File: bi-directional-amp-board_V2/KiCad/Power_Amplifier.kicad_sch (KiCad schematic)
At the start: 23 parts

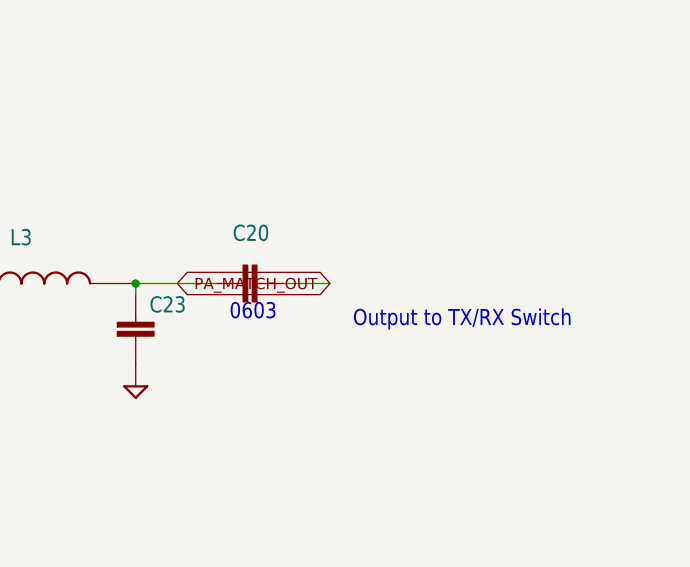
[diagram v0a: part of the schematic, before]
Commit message: re importing eagle files to kicad
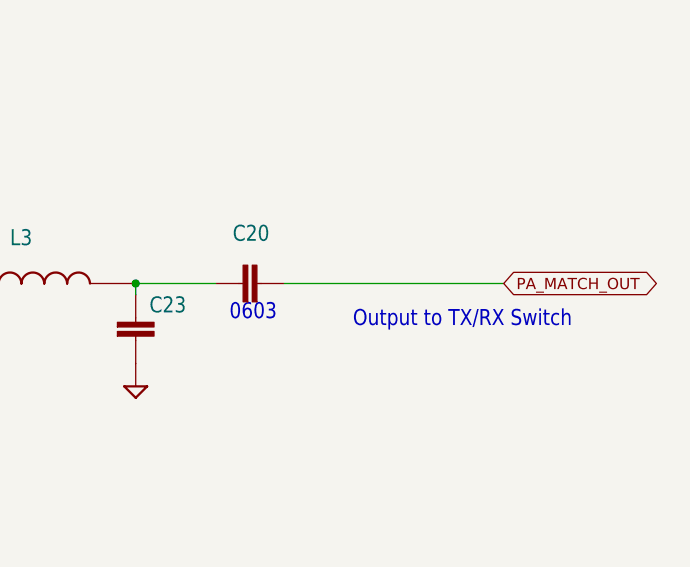
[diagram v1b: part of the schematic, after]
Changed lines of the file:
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@@
 (kicad_sch (version 20211123) (generator eeschema)
-  (paper "User" 490.22 254.406)
+  (paper "A2")
   (junction (at 105.918 114.3) (diameter 0) (color 0 0 0 0)
   )
@@
     (stroke (width 0) (type default) (color 0 0 0 0))
   )
-  (wire (pts (xy 219.456 114.3) (xy 224.536 114.3))
+  (wire (pts (xy 219.456 114.3) (xy 243.84 114.3))
     (stroke (width 0) (type default) (color 0 0 0 0))
   )
@@
     (effects (font (size 1.778 1.5113)) (justify left bottom))
   )
-  (global_label "PA_MATCH_OUT" (shape bidirectional) (at 224.536 114.3 180) (fields_autoplaced)
-    (effects (font (size 1.2446 1.2446)) (justify right))
-    (property "Intersheet References" "${INTERSHEET_REFS}" (id 0) (at 413.512 0 0)
+  (global_label "PA_MATCH_OUT" (shape bidirectional) (at 243.84 114.3 0) (fields_autoplaced)
+    (effects (font (size 1.2446 1.2446)) (justify left))
+    (property "Intersheet References" "${INTERSHEET_REFS}" (id 0) (at 54.864 228.6 0)
       (effects (font (size 1.27 1.27)) hide)
     )

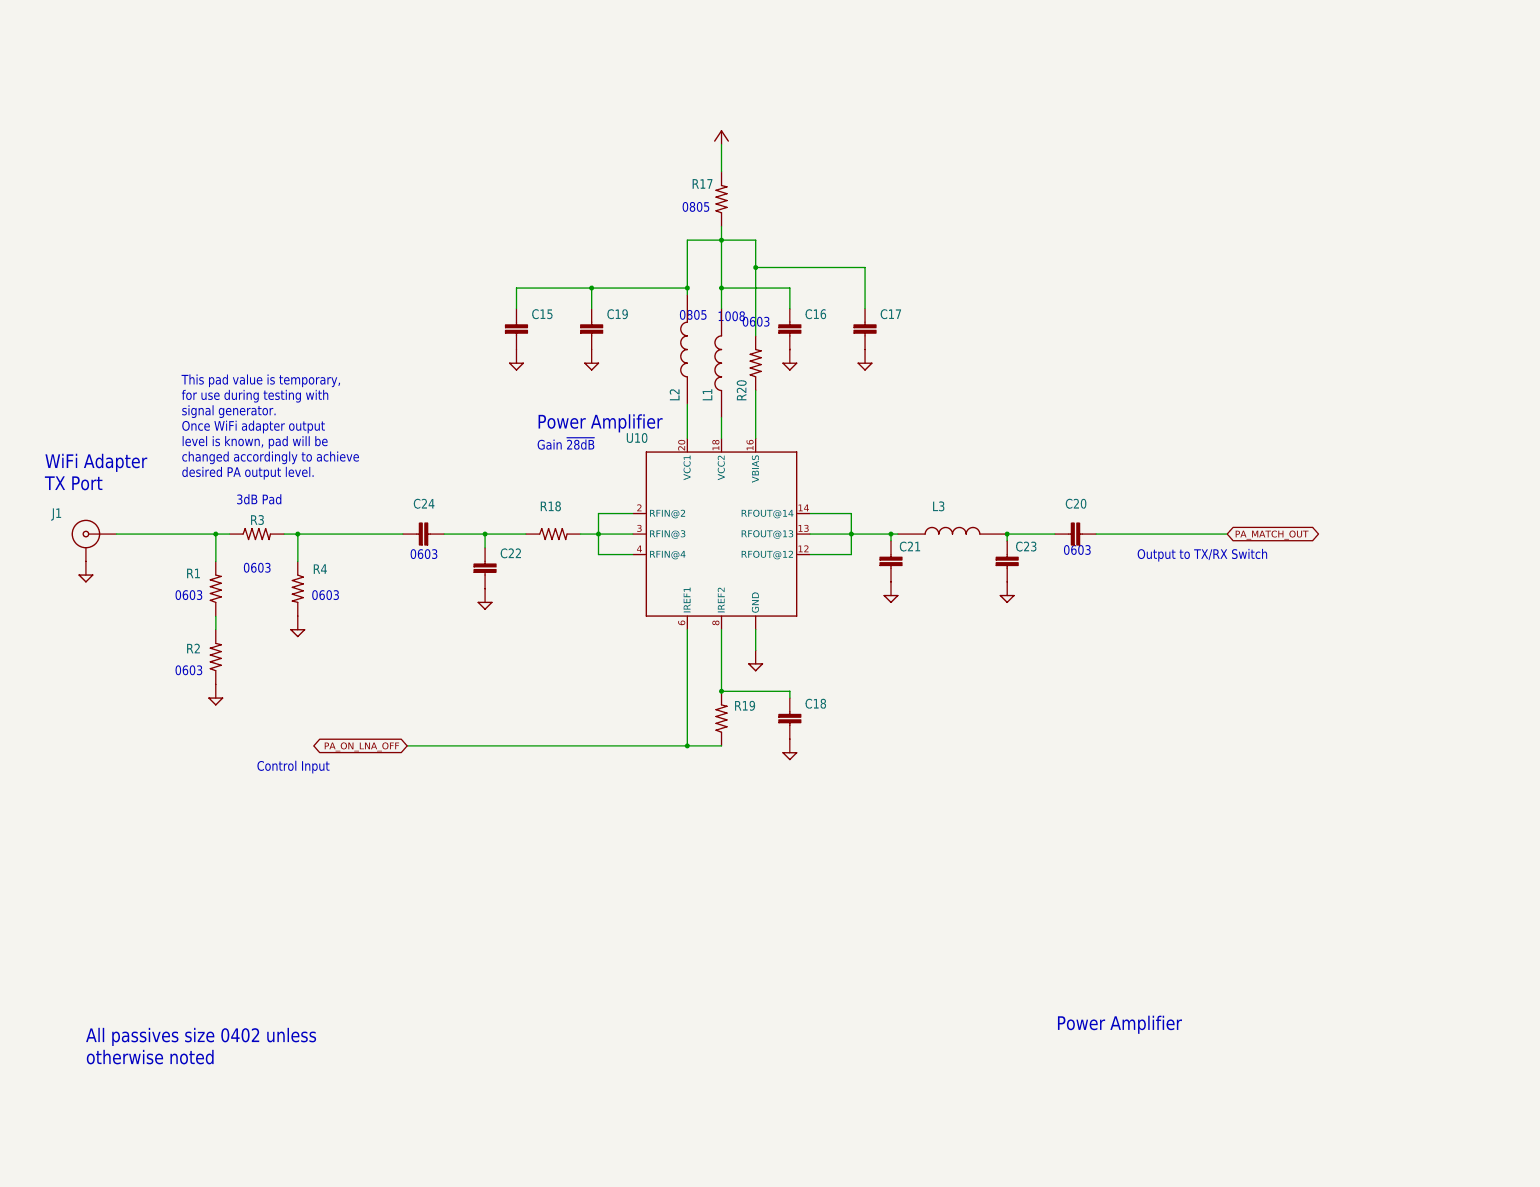
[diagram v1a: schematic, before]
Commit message: Updated KiCAD import of bidirectional amplifier. Still a bit broken, but better now.
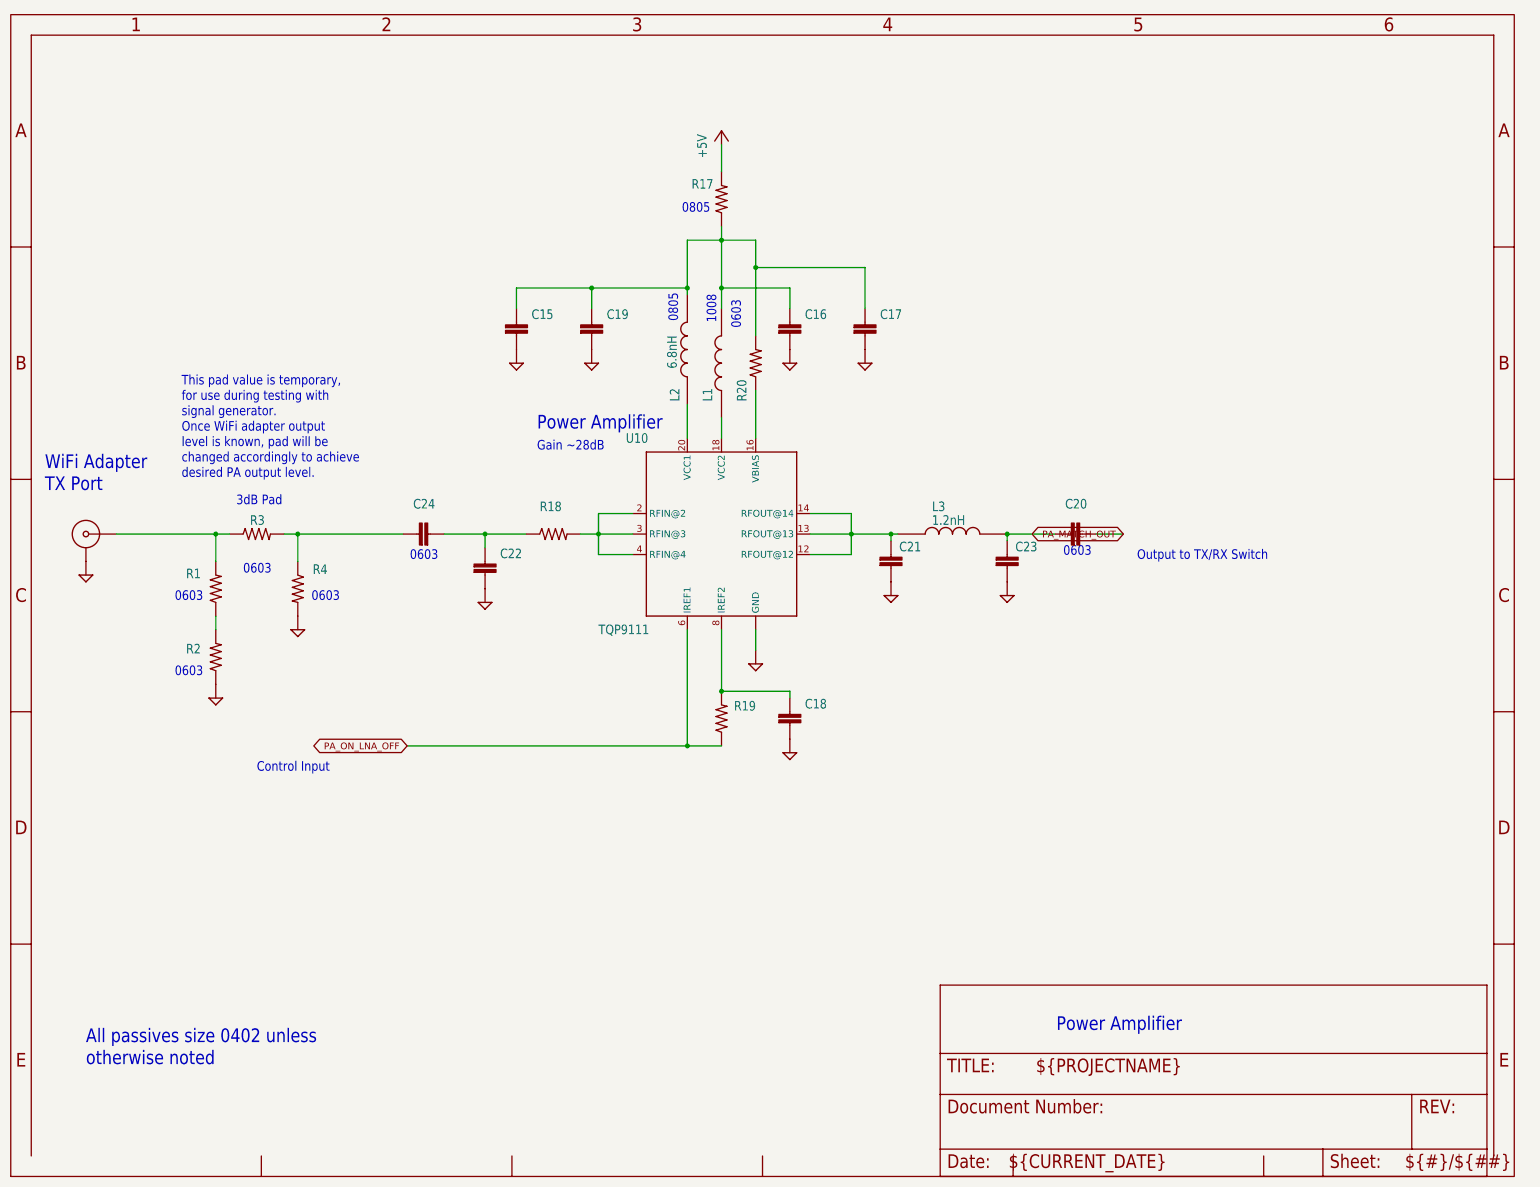
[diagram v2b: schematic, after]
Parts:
- C15, C16, C17: value (none) -> C-EU0402-B-NOSILK; footprint (none) -> Bidirectional_Amp:.0402-B-NOSILK; MFR (none) -> TDK; MPN (none) -> CGA2B1X7R1C104K050BC
- C18: value (none) -> C-EU0402-B-NOSILK; footprint (none) -> Bidirectional_Amp:.0402-B-NOSILK; MFR (none) -> Murata; MPN (none) -> GCM1555C1H101JA16D
- C19: value (none) -> C-EU0402-B-NOSILK; footprint (none) -> Bidirectional_Amp:.0402-B-NOSILK; MFR (none) -> TDK; MPN (none) -> CGA2B2NP01H102J050BA
- C20: value (none) -> C-EU0603-C-NOSILK; footprint (none) -> Bidirectional_Amp:.0603-C-NOSILK; MFR (none) -> Murata; MPN (none) -> GCM1885C1H101JA16D
- C21: value (none) -> C-EU0402-C-NOSILK; footprint (none) -> Bidirectional_Amp:.0402-C-NOSILK; MFR (none) -> Taiyo Yuden; MPN (none) -> UVK105CG030JW-F
- C22: value (none) -> C-EU0402-C-NOSILK; footprint (none) -> Bidirectional_Amp:.0402-C-NOSILK; MFR (none) -> Taiyo Yuden; MPN (none) -> UVK105CG2R2JW-F
- C23: value (none) -> C-EU0402-C-NOSILK; footprint (none) -> Bidirectional_Amp:.0402-C-NOSILK; MFR (none) -> Murata; MPN (none) -> GJM1555C1H1R6BB01D
- C24: value (none) -> C-EU0603-C-NOSILK; footprint (none) -> Bidirectional_Amp:.0603-C-NOSILK; MFR (none) -> AVX Corp.; MPN (none) -> 06032U4R7BAT2A
- J1: value (none) -> 142-0701-851_ALT; footprint (none) -> Bidirectional_Amp:142-0701-851; MFR (none) -> Cinch; MPN (none) -> 142-0701-851
- L1: value (none) -> 1008HQ-10NXJLB1008_IMPERIAL_2520_METRIC; footprint (none) -> Bidirectional_Amp:INDC2520X120N; MFR (none) -> COILCRAFT; MPN (none) -> 1008HQ-10NXJLB
- L2: value (none) -> 6.8nH; footprint (none) -> Bidirectional_Amp:0805CS
- L3: value (none) -> 1.2nH; footprint (none) -> Bidirectional_Amp:0402CS1N2XJLW
- R1, R2: value (none) -> R-US_0603-C-NOSILK; footprint (none) -> Bidirectional_Amp:.0603-C-NOSILK; MFR (none) -> Panasonic; MPN (none) -> ERJ-3EKF1470V
- R17: value (none) -> R-US_R0805; footprint (none) -> Bidirectional_Amp:R0805; MFR (none) -> Panasonic; MPN (none) -> ERJ-6GEY0R00V
- R18: value (none) -> R-US_R0402; footprint (none) -> Bidirectional_Amp:R0402; MFR (none) -> Panasonic; MPN (none) -> ERJ-2GEJ1R2X
- R19: value (none) -> R-US_0402-B-NOSILK; footprint (none) -> Bidirectional_Amp:.0402-B-NOSILK; MFR (none) -> Panasonic; MPN (none) -> ERJ-2RKF1100X
- R20: value (none) -> R-US_0603-C-NOSILK; footprint (none) -> Bidirectional_Amp:.0603-C-NOSILK; MFR (none) -> Panasonic; MPN (none) -> ERJ-3EKF2200V
- R3: value (none) -> R-US_0603-C-NOSILK; footprint (none) -> Bidirectional_Amp:.0603-C-NOSILK; MFR (none) -> Panasonic; MPN (none) -> ERJ-3EKF17R8V
- R4: value (none) -> R-US_0603-C-NOSILK; footprint (none) -> Bidirectional_Amp:.0603-C-NOSILK; MFR (none) -> Panasonic; MPN (none) -> ERJ-3EKF2940V
- U10: value (none) -> TQP9111; footprint (none) -> Bidirectional_Amp:QFN50P400X400X102-21N
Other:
- note added: "Gain ~28dB"
- note removed: "Gain ~{28dB}"
